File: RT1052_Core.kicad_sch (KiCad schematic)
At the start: 2 parts, among them U1 M1052-16F128AWI-T

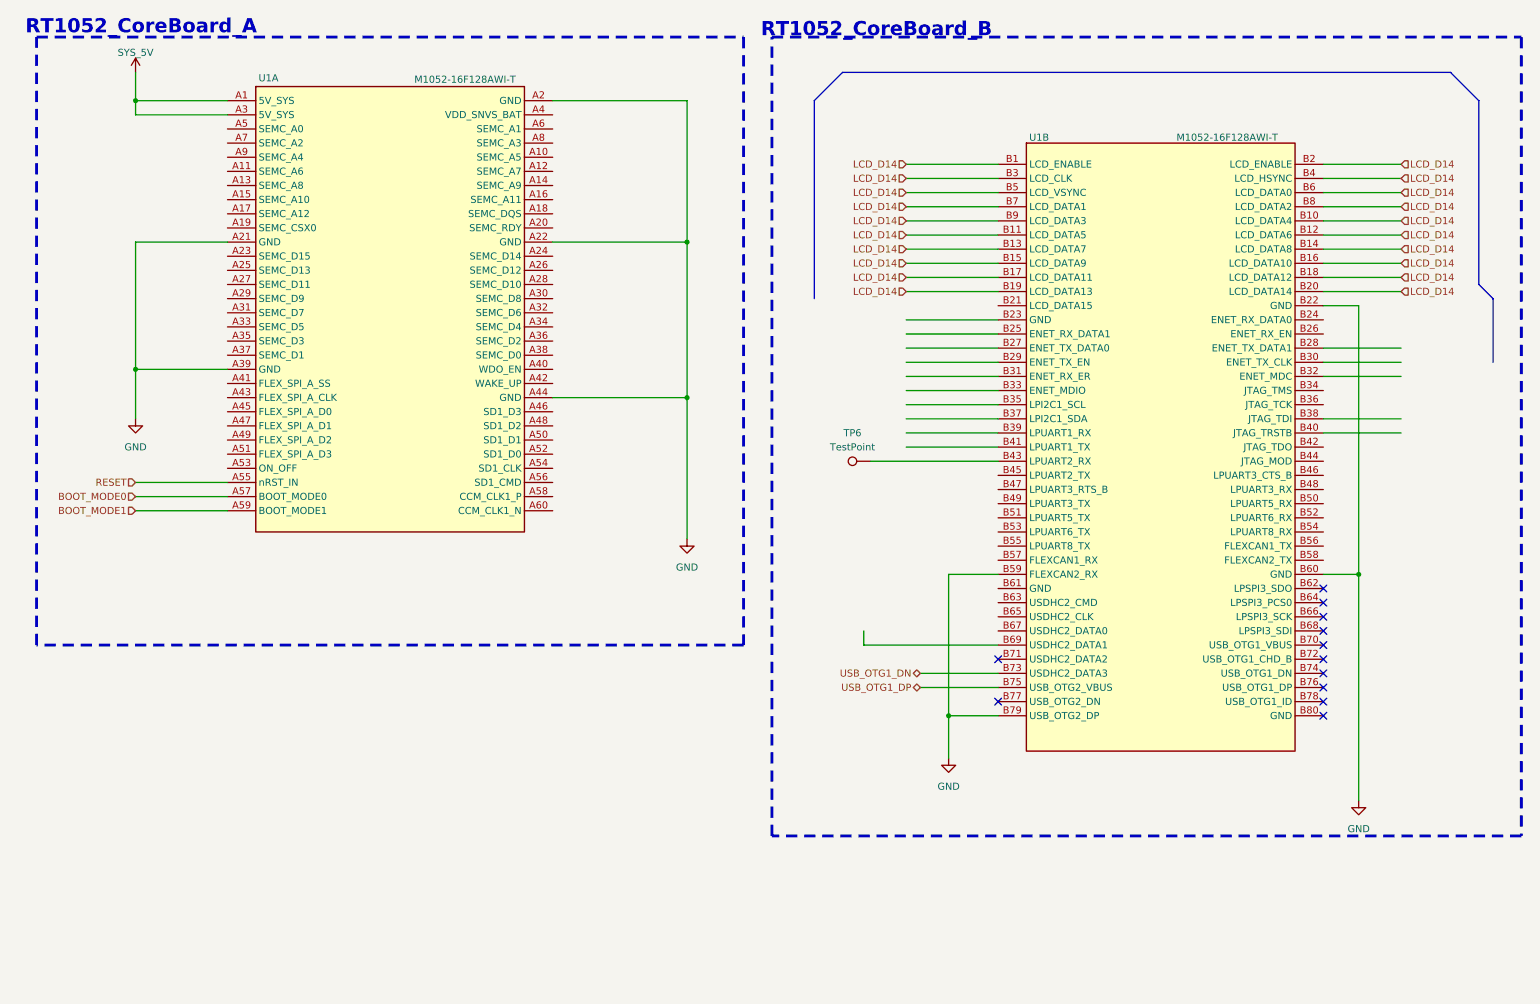
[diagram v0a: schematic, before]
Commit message: 2026 08 16 原理图完成，下一步制作分配未完成的器件封装，准备layout
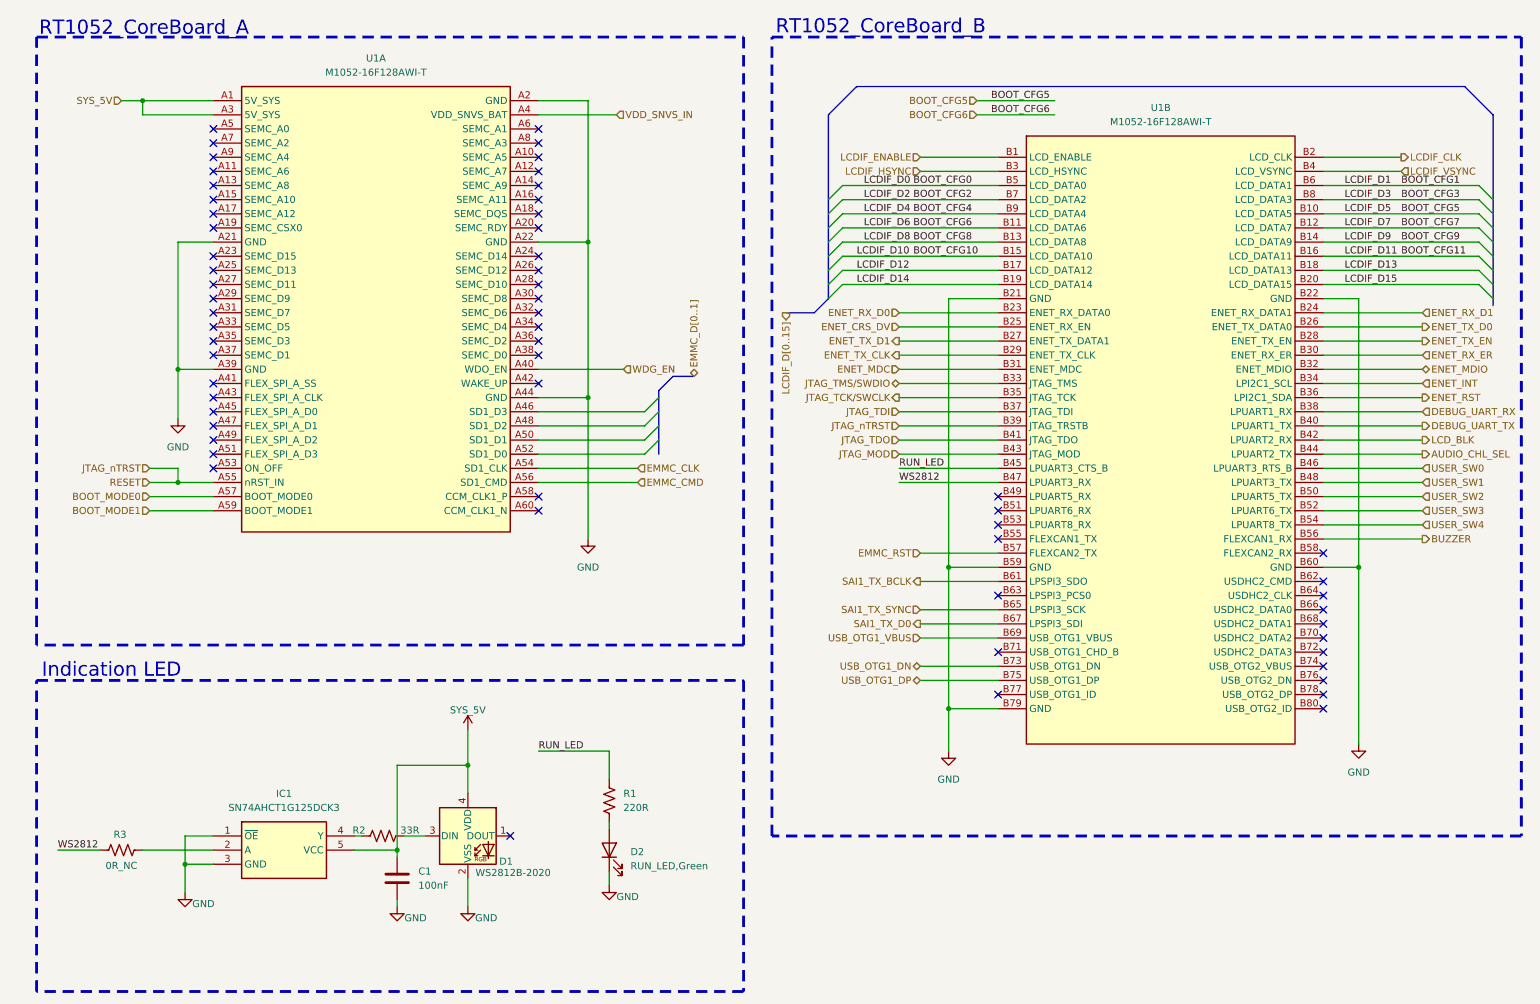
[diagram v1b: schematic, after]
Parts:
- removed TP6: TestPoint, symbol Connector:TestPoint
- added C1: 100nF, Capacitor_SMD:C_0603_1608Metric_Pad1.08x0.95mm_HandSolder, symbol Device:C
- added D1: WS2812B-2020, LED_SMD:LED_RGB_1210, symbol LED:WS2812B-2020
- added D2: RUN_LED,Green, Capacitor_SMD:C_0805_2012Metric_Pad1.18x1.45mm_HandSolder, symbol Device:LED
- added IC1: SN74AHCT1G125DCK3, UPT:SOT65P210X110-5N, symbol UPT:SN74AHCT1G125DCK3
- added R1: 220R, Resistor_SMD:R_0603_1608Metric_Pad0.98x0.95mm_HandSolder, symbol Device:R_US
- added R2: 33R, Resistor_SMD:R_0603_1608Metric_Pad0.98x0.95mm_HandSolder, symbol Device:R_US
- added R3: 0R_NC, Resistor_SMD:R_0603_1608Metric_Pad0.98x0.95mm_HandSolder, symbol Device:R_US
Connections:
- net RESET is gone; now on net JTAG_nTRST: U1.A55 (nRST_IN)
- net GND: now also U1.B21 (GND), C1.2, D1.2 (VSS), D2.1 (K), IC1.1 (~{OE}), IC1.3 (GND)
- net SYS_5V: now also C1.1, D1.4 (VDD), IC1.5 (VCC)
- net JTAG_MOD: now reaches U1.B43 (JTAG_MOD)
- net VDD_SNVS_IN: now reaches U1.A4 (VDD_SNVS_BAT)
- net WDG_EN: now reaches U1.A40 (WDO_EN)
- net EMMC_CLK: now reaches U1.A54 (SD1_CLK)
- net EMMC_CMD: now reaches U1.A56 (SD1_CMD)
- net ENET_RX_D0: now reaches U1.B23 (ENET_RX_DATA0)
- net ENET_RX_D1: now reaches U1.B24 (ENET_RX_DATA1)
- net ENET_CRS_DV: now reaches U1.B25 (ENET_RX_EN)
- net ENET_TX_D0: now reaches U1.B26 (ENET_TX_DATA0)
- net ENET_TX_D1: now reaches U1.B27 (ENET_TX_DATA1)
- net ENET_TX_EN: now reaches U1.B28 (ENET_TX_EN)
- net ENET_TX_CLK: now reaches U1.B29 (ENET_TX_CLK)
- net ENET_RX_ER: now reaches U1.B30 (ENET_RX_ER)
- net ENET_MDC: now reaches U1.B31 (ENET_MDC)
- net ENET_MDIO: now reaches U1.B32 (ENET_MDIO)
- net JTAG_TMS/SWDIO: now reaches U1.B33 (JTAG_TMS)
- net ENET_INT: now reaches U1.B34 (LPI2C1_SCL)
- net JTAG_TCK/SWCLK: now reaches U1.B35 (JTAG_TCK)
- net ENET_RST: now reaches U1.B36 (LPI2C1_SDA)
- net JTAG_TDI: now reaches U1.B37 (JTAG_TDI)
- net DEBUG_UART_RX: now reaches U1.B38 (LPUART1_RX)
- net JTAG_nTRST: now reaches U1.B39 (JTAG_TRSTB)
- net DEBUG_UART_TX: now reaches U1.B40 (LPUART1_TX)
- net JTAG_TDO: now reaches U1.B41 (JTAG_TDO)
- net LCD_BLK: now reaches U1.B42 (LPUART2_RX)
- net AUDIO_CHL_SEL: now reaches U1.B44 (LPUART2_TX)
- net RUN_LED: now reaches U1.B45 (LPUART3_CTS_B)
- net RUN_LED: now also R1.1
- net USER_SW0: now reaches U1.B46 (LPUART3_RTS_B)
- net WS2812: now reaches U1.B47 (LPUART3_RX)
- net WS2812: now also R3.1
- net USER_SW1: now reaches U1.B48 (LPUART3_TX)
- net USER_SW2: now reaches U1.B50 (LPUART5_TX)
- net USER_SW3: now reaches U1.B52 (LPUART6_TX)
- net USER_SW4: now reaches U1.B54 (LPUART8_TX)
- net BUZZER: now reaches U1.B56 (FLEXCAN1_RX)
- net EMMC_RST: now reaches U1.B57 (FLEXCAN2_TX)
- net SAI1_TX_BCLK: now reaches U1.B61 (LPSPI3_SDO)
- net SAI1_TX_SYNC: now reaches U1.B65 (LPSPI3_SCK)
- net SAI1_TX_D0: now reaches U1.B67 (LPSPI3_SDI)
- net USB_OTG1_VBUS: now reaches U1.B69 (USB_OTG1_VBUS)
- removed net LCD_D14: U1.B1 (LCD_ENABLE), U1.B10 (LCD_DATA4), U1.B11 (LCD_DATA5), U1.B12 (LCD_DATA6), U1.B13 (LCD_DATA7), U1.B14 (LCD_DATA8), U1.B15 (LCD_DATA9), U1.B16 (LCD_DATA10), U1.B17 (LCD_DATA11), U1.B18 (LCD_DATA12), U1.B19 (LCD_DATA13), U1.B2 (LCD_ENABLE), U1.B20 (LCD_DATA14), U1.B3 (LCD_CLK), U1.B4 (LCD_HSYNC), U1.B5 (LCD_VSYNC), U1.B6 (LCD_DATA0), U1.B7 (LCD_DATA1), U1.B8 (LCD_DATA2), U1.B9 (LCD_DATA3)
- new net: IC1.2 (A), R3.2
- new net: D1.3 (DIN), R2.2
- new net: IC1.4 (Y), R2.1
- new net: D2.2 (A), R1.2
- new net BOOT_CFG0: U1.B5 (LCD_DATA0)
- new net BOOT_CFG1: U1.B6 (LCD_DATA1)
- new net BOOT_CFG10: U1.B15 (LCD_DATA10)
- new net BOOT_CFG11: U1.B16 (LCD_DATA11)
- new net BOOT_CFG2: U1.B7 (LCD_DATA2)
- new net BOOT_CFG3: U1.B8 (LCD_DATA3)
- new net BOOT_CFG4: U1.B9 (LCD_DATA4)
- new net BOOT_CFG5: U1.B10 (LCD_DATA5)
- new net BOOT_CFG6: U1.B11 (LCD_DATA6)
- new net BOOT_CFG7: U1.B12 (LCD_DATA7)
- new net BOOT_CFG8: U1.B13 (LCD_DATA8)
- new net BOOT_CFG9: U1.B14 (LCD_DATA9)
- new net LCDIF_CLK: U1.B2 (LCD_CLK)
- new net LCDIF_D12: U1.B17 (LCD_DATA12)
- new net LCDIF_D13: U1.B18 (LCD_DATA13)
- new net LCDIF_D14: U1.B19 (LCD_DATA14)
- new net LCDIF_D15: U1.B20 (LCD_DATA15)
- new net LCDIF_ENABLE: U1.B1 (LCD_ENABLE)
- new net LCDIF_HSYNC: U1.B3 (LCD_HSYNC)
- new net LCDIF_VSYNC: U1.B4 (LCD_VSYNC)
- no-connect marks 12 -> 61
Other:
- note added: "Indication LED"

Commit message: 2026 08 24 画图完成，准备生产
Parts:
- U1: footprint (none) -> UPT:M1052-16F128AWI-T
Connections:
- net AUDIO_CHL_SEL: now also U1.B53 (LPUART8_RX); no longer U1.B44 (LPUART2_TX)
- net BUZZER: now also U1.B72 (USDHC2_DATA3); no longer U1.B56 (FLEXCAN1_RX)
- net EMMC_RST: now also U1.B45 (LPUART3_CTS_B); no longer U1.B57 (FLEXCAN2_TX)
- net LCD_BLK: now also U1.B55 (FLEXCAN1_TX); no longer U1.B42 (LPUART2_RX)
- net RUN_LED: now also U1.B47 (LPUART3_RX); no longer U1.B45 (LPUART3_CTS_B)
- net USER_SW0: now also U1.B62 (USDHC2_CMD); no longer U1.B46 (LPUART3_RTS_B)
- net USER_SW1: now also U1.B64 (USDHC2_CLK); no longer U1.B48 (LPUART3_TX)
- net USER_SW2: now also U1.B66 (USDHC2_DATA0); no longer U1.B50 (LPUART5_TX)
- net USER_SW3: now also U1.B68 (USDHC2_DATA1); no longer U1.B52 (LPUART6_TX)
- net USER_SW4: now also U1.B70 (USDHC2_DATA2); no longer U1.B54 (LPUART8_TX)
- net WS2812: now also U1.B51 (LPUART6_RX); no longer U1.B47 (LPUART3_RX)
- net EMMC_D3: now reaches U1.A46 (SD1_D3)
- net EMMC_D2: now reaches U1.A48 (SD1_D2)
- net EMMC_D1: now reaches U1.A50 (SD1_D1)
- net EMMC_D0: now reaches U1.A52 (SD1_D0)
- net LCD_RST: now reaches U1.B49 (LPUART5_RX)
- net ENET_TX_CLK renamed ENET_CLK
- no-connect marks 61 -> 60
